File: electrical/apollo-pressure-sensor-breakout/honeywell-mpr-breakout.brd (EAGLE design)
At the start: 25 x 30 mm, 8 parts, among them U1 HONEYWELL-MPR-SMD-GAUGE, X1 RJ45-8-2-CONEC-1, X2 M04X2

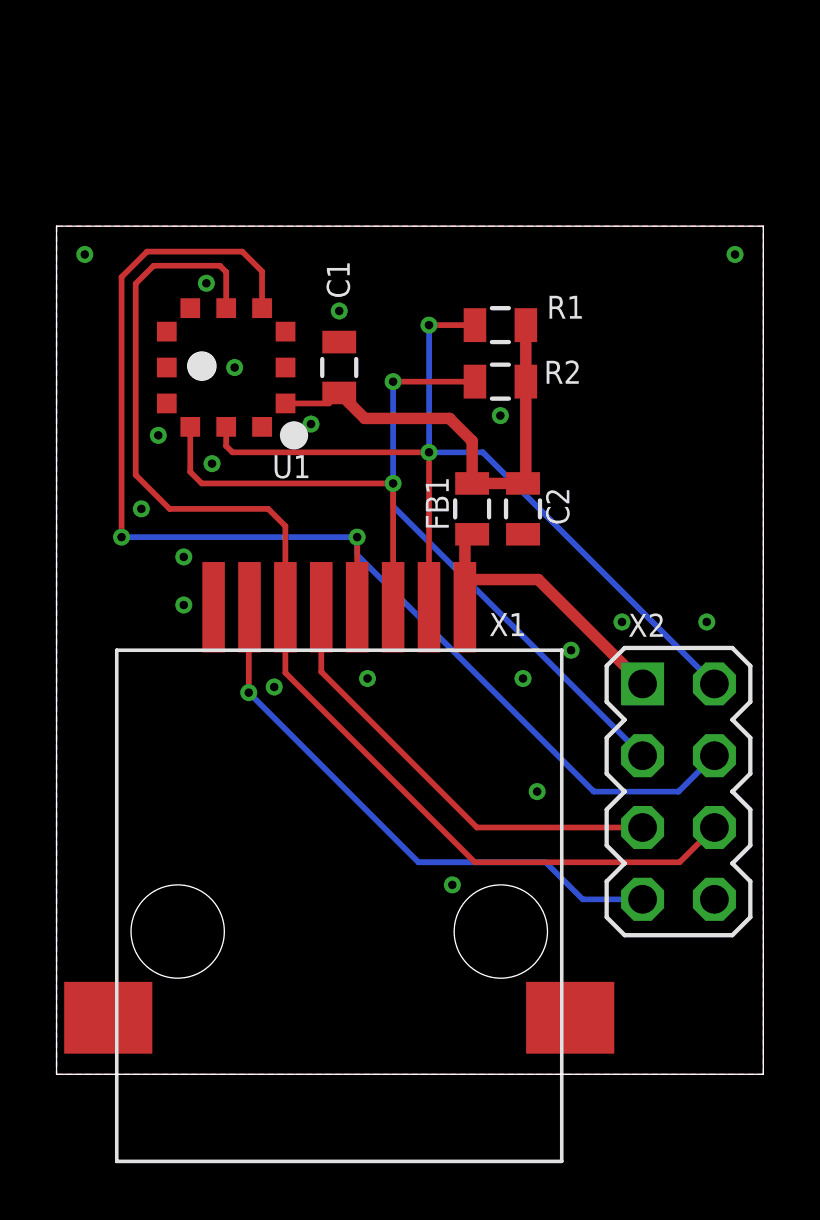
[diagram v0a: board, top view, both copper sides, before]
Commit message: add Gerber/SMTA order info for JLCPCB
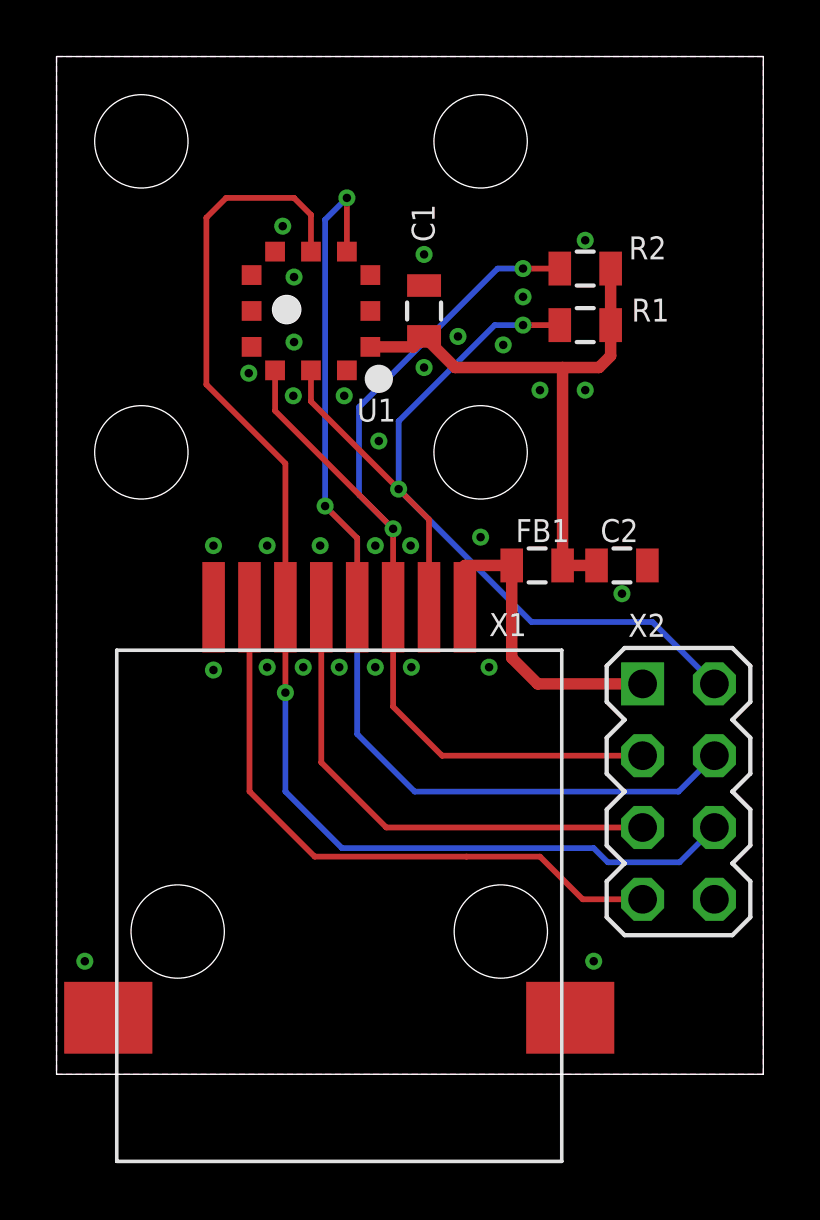
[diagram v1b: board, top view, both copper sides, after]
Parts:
- added JP1, JP2, JP3, JP4: STAND-OFF, apollo-ctrl:STAND-OFF
- moved R2 5.00 mm to (18.7, 28.5)
- moved C2 4.03 mm to (20.0, 18.0), turned to 0 degrees
- moved C1 3.61 mm to (13.0, 27.0)
- moved U1 3.61 mm to (9.00, 27.0)
- moved FB1 3.05 mm to (17.0, 18.0), turned to 0 degrees
- moved R1 3.00 mm to (18.7, 26.5)
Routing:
- net RES: track 44.2 -> 39.7 mm
- net 3.3V: track 16.5 -> 20.6 mm
- net SCL: track 33.1 -> 37.1 mm
- net AUX1: track 41.3 -> 43.7 mm, vias 0 -> 1
- net AUX2: track 20.0 -> 22.0 mm, vias 1 -> 0
- net CS: track 15.9 -> 17.8 mm
- net SDA: track 33.0 -> 33.6 mm
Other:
- board size 25 x 30 mm -> 25 x 36 mm
